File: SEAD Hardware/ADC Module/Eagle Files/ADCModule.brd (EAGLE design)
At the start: 48.9 x 67.6 mm, 51 parts, among them U1 ADS8568_PM_64, U2 LP2950-3.3ACZ

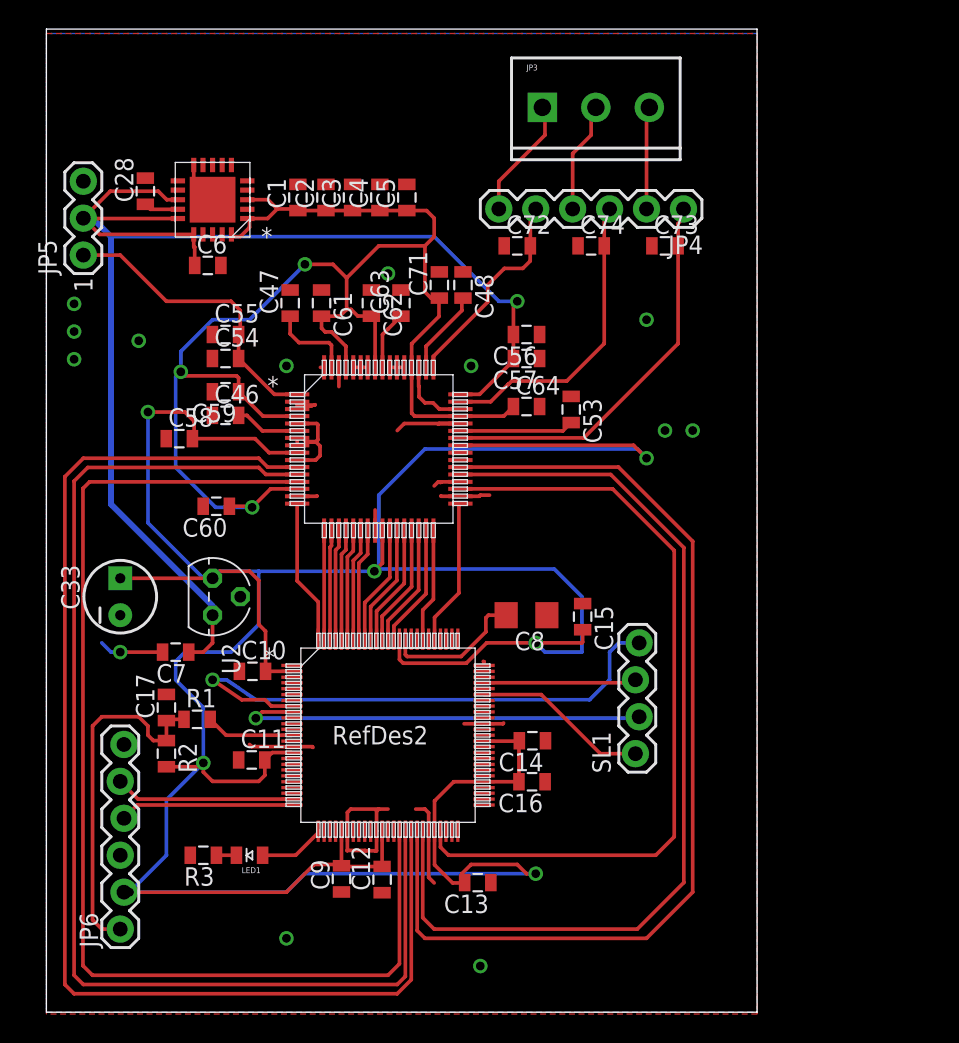
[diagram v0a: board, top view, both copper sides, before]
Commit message: Finished ADC Module v1.2 and reorganized file directories.
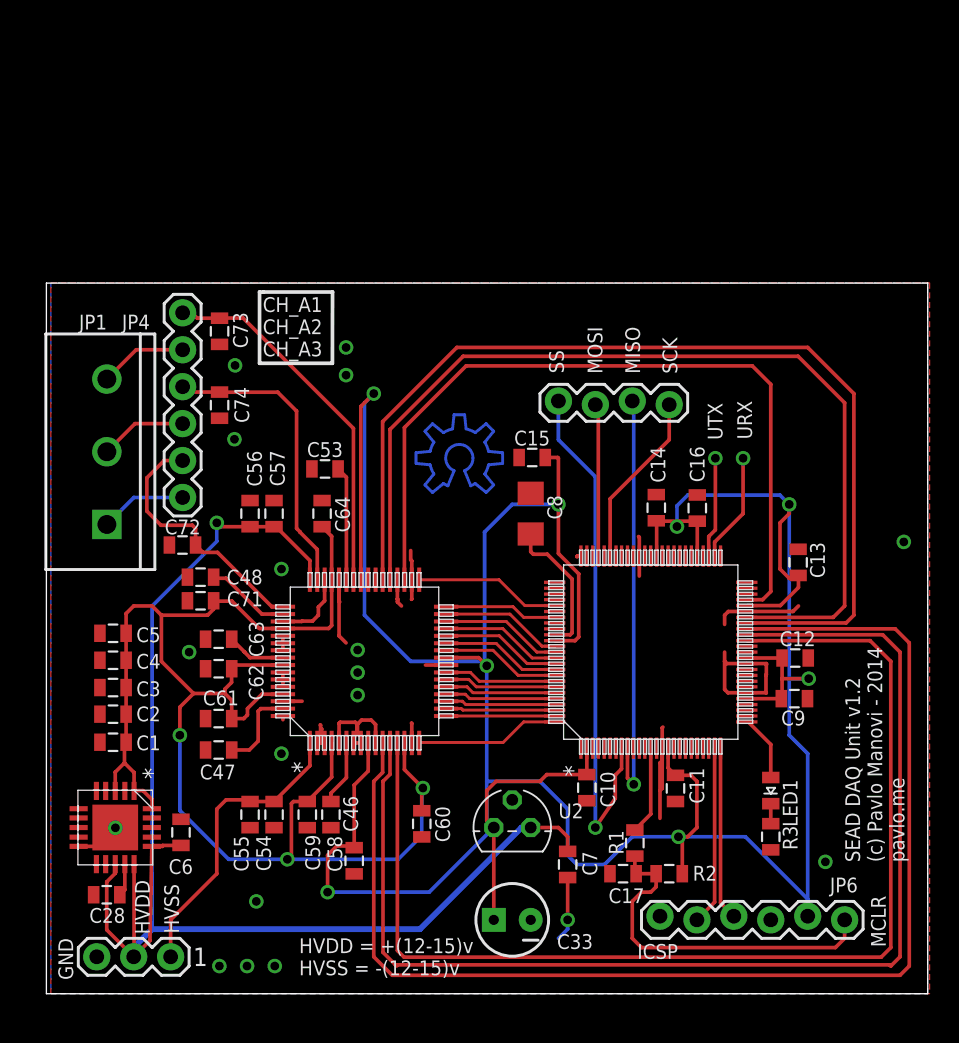
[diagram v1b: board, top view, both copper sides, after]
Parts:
- removed JP3: M03SCREW_LOCK, ASL:SCREWTERMINAL-3.5MM-3_LOCK.007S
- added JP1: M03-SCREW-5MM, ASL:SCREWTERMINAL-5MM-3
- moved JP5 50.9 mm to (6.00, 2.54), turned to 180 degrees
- moved JP6 49.8 mm to (54.9, 5.08), turned to 180 degrees
- moved C28 48.5 mm to (4.15, 6.81), turned to 180 degrees
- moved U$3 43.7 mm to (4.74, 11.4), turned to 270 degrees
- moved C1 39.6 mm to (4.58, 17.3), turned to 180 degrees
- moved R3 39.0 mm to (49.8, 10.8), turned to 270 degrees
- moved C6 39.0 mm to (9.26, 11.1), turned to 90 degrees
- moved C2 38.4 mm to (4.58, 19.2), turned to 180 degrees
- moved C3 37.5 mm to (4.58, 21.1), turned to 180 degrees
- moved C4 36.7 mm to (4.58, 22.9), turned to 180 degrees
- moved C5 36.1 mm to (4.58, 24.8), turned to 180 degrees
- moved LED1 36.1 mm to (49.8, 14.0), turned to 270 degrees
- moved R2 35.6 mm to (42.8, 8.26), turned to 0 degrees
- moved C33 34.9 mm to (32.0, 5.08), turned to 180 degrees
- moved C9 33.5 mm to (51.4, 20.3), turned to 180 degrees
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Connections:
- new net RX1A: U$1.52
- new net TX1A: U$1.53
- net N$1: now also JP1.3; no longer JP3.3
- net N$2: now also JP1.2; no longer JP3.2
- net N$3: now also JP1.1; no longer JP3.1
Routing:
- net N$5: track 0.00 -> 28.4 mm
- net VDD3V3_D: track 252.0 -> 237.1 mm, vias 7 -> 8
- net RX1A: track 0.00 -> 7.54 mm, vias 0 -> 1
- net TX1A: track 0.00 -> 6.92 mm, vias 0 -> 1
- net GND: track 66.2 -> 71.2 mm, vias 13 -> 18
- net AA3_R_OUT: track 14.6 -> 18.0 mm
- net N$3: track 8.37 -> 5.98 mm
- net SS: track 38.6 -> 36.5 mm
- net N$2: track 7.65 -> 6.01 mm
- net AA1_R_OUT: track 27.1 -> 25.5 mm
- net VDD5V0_A: track 104.8 -> 106.0 mm
- net N$1: track 7.06 -> 6.04 mm
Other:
- board size 48.9 x 67.6 mm -> 60.6 x 48.9 mm
- board text added: "CH_A1 CH_A2 CH_A3"
- board text added: "GND"
- board text added: "HVDD"
- board text added: "HVDD = +(12-15)v HVSS = -(12-15)v"
- board text added: "HVSS"
- board text added: "ICSP"
- board text added: "MCLR"
- board text added: "MISO"
- board text added: "MOSI"
- board text added: "Released under the TAPR OHL v1.0 - http://www.tapr.org/OHL"
- board text added: "SCK"
- board text added: "SEAD DAQ Unit v1.2 (c) Pavlo Manovi - 2014 pavlo.me"
- board text added: "SS"
- board text added: "URX"
- board text added: "UTX"

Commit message: Started SPI/USB Bridge
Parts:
- added C18: 10nF, SensorCape:0805
- added C19, C20: 47pF, SensorCape:0805
- added C21, C23, C24: 100nF, SensorCape:0805
- added C22: 4.7uF, SensorCape:CPOL-RADIAL-10UF-25V
- added L1: Ferrite Bead 0805, ASL:0805
- added R4, R5: 27 1%, SensorCape:0805
- added U$2: FT121Q, SensorCape:QFN16
- added U3: SI8663BC-B-IS1, SensorCape:SOIC-16
- added X1: MINI-USB-SCHIELD-32005-201, con-cypressindustries:32005-201
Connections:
- new net GND_USB: C18.2, C19.1, C20.2, C21.1, C22.2, C23.1, U$2.12, U$2.2, U3.8, X1.5
- new net N$10: R4.2, U$2.13
- new net N$11: X1.M1, X1.M2, X1.M3, X1.M4
- new net N$12: R5.2, U$2.14
- new net N$13: U$2.6, U3.4
- new net N$17: U$2.7, U3.7
- new net N$18: U$2.16, U3.5
- new net N$6: C18.1, L1.1, X1.1
- new net N$8: C19.2, R4.1, X1.2
- new net N$9: C20.1, R5.1, X1.3
- new net SCLK: U3.12
- new net VCC3V3_USB: C21.2, C24.1, C24.2, U$2.10, U$2.3, U$2.8, U$2.9, U3.1
- new net VCC_USB: C22.1, C23.2, L1.2, U$2.11
- net MISO: now also U3.13
- net MOSI: now also U3.10
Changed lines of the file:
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@@
 <layer number="97" name="Info" color="7" fill="1" visible="no" active="no"/>
 <layer number="98" name="Guide" color="6" fill="1" visible="no" active="no"/>
+<layer number="99" name="SpiceOrder" color="5" fill="1" visible="no" active="no"/>
 <layer number="100" name="Muster" color="7" fill="1" visible="no" active="no"/>
 <layer number="101" name="Patch_Top" color="12" fill="4" visible="yes" active="yes"/>
@@
 <attribute name="VALUE" x="2.89" y="31.005" size="0.4064" layer="27" rot="R90"/>
 </element>
+<element name="U$2" library="SensorCape" package="QFN16" value="FT121Q" x="-5.29" y="4.42"/>
+<element name="U3" library="SensorCape" package="SOIC-16" value="SI8663BC-B-IS1" x="-11.52" y="4.88"/>
+<element name="X1" library="con-cypressindustries" package="32005-201" value="MINI-USB-SCHIELD-32005-201" x="-20.7" y="7.35">
+<attribute name="OC_NEWARK" value="unknown" x="-20.7" y="7.35" size="1.778" layer="27" display="off"/>
+<attribute name="MPN" value="" x="-20.7" y="7.35" size="1.778" layer="27" display="off"/>
+<attribute name="MF" value="" x="-20.7" y="7.35" size="1.778" layer="27" display="off"/>
+<attribute name="OC_FARNELL" value="unknown" x="-20.7" y="7.35" size="1.778" layer="27" display="off"/>
+</element>
+<element name="L1" library="ASL" package="0805" value="Ferrite Bead 0805" x="-25.14" y="-2.68"/>
+<element name="C18" library="SensorCape" package="0805" value="10nF" x="-25.14" y="-6.23"/>
+<element name="R4" library="SensorCape" package="0805" value="27 1%" x="-25.14" y="-16.88"/>
+<element name="R5" library="SensorCape" package="0805" value="27 1%" x="-25.14" y="-20.43"/>
+<element name="C22" library="SensorCape" package="CPOL-RADIAL-10UF-25V" value="4.7uF" x="-32.13" y="-20.8"/>
+<element name="C23" library="SensorCape" package="0805" value="100nF" x="-33.2" y="-27.53"/>
+<element name="C19" library="SensorCape" package="0805" value="47pF" x="-33.2" y="-31.08"/>
+<element name="C20" library="SensorCape" package="0805" value="47pF" x="-33.2" y="-34.63"/>
+<element name="C21" library="SensorCape" package="0805" value="100nF" x="-33.2" y="-38.18"/>
+<element name="C24" library="SensorCape" package="0805" value="100nF" x="-33.2" y="-42.62"/>
 </elements>
 <signals>
@@
 <wire x1="37.9582" y1="30.099" x2="37.9582" y2="40.3098" width="0.254" layer="1"/>
 <wire x1="37.9582" y1="40.3098" x2="37.755" y2="40.513" width="0.254" layer="1"/>
+<contactref element="U3" pad="10"/>
+<wire x1="-8.8276" y1="1.705" x2="37.9582" y2="30.099" width="0" layer="19" extent="1-1"/>
 </signal>
 <signal name="MISO">
@@
 <wire x1="40.3966" y1="14.4018" x2="40.3966" y2="40.6654" width="0.254" layer="16"/>
 <wire x1="40.3966" y1="40.6654" x2="40.295" y2="40.767" width="0.254" layer="16"/>
+<contactref element="U3" pad="13"/>
+<wire x1="-8.8276" y1="5.515" x2="39.9648" y2="14.8336" width="0" layer="19" extent="1-1"/>
 </signal>
 <signal name="SS">
@@
 <wire x1="28.041234375" y1="35.9738625" x2="27.610715625" y2="34.9345" width="0.2" layer="16"/>
 </signal>
+<signal name="N$6">
+<contactref element="X1" pad="1"/>
+<contactref element="L1" pad="1"/>
+<contactref element="C18" pad="1"/>
+<wire x1="-26.04" y1="-2.68" x2="-26.04" y2="-6.23" width="0" layer="19" extent="1-1"/>
+<wire x1="-17.7" y1="8.95" x2="-26.04" y2="-2.68" width="0" layer="19" extent="1-1"/>
+</signal>
+<signal name="N$8">
+<contactref element="X1" pad="2"/>
+<contactref element="R4" pad="1"/>
+<contactref element="C19" pad="2"/>
+<wire x1="-26.04" y1="-16.88" x2="-32.3" y2="-31.08" width="0" layer="19" extent="1-1"/>
+<wire x1="-17.7" y1="8.15" x2="-26.04" y2="-16.88" width="0" layer="19" extent="1-1"/>
+</signal>
+<signal name="N$9">
+<contactref element="X1" pad="3"/>
+<contactref element="R5" pad="1"/>
+<contactref element="C20" pad="1"/>
+<wire x1="-26.04" y1="-20.43" x2="-34.1" y2="-34.63" width="0" layer="19" extent="1-1"/>
+<wire x1="-17.7" y1="7.35" x2="-26.04" y2="-20.43" width="0" layer="19" extent="1-1"/>
+</signal>
+<signal name="N$11">
+<contactref element="X1" pad="M4"/>
+<contactref element="X1" pad="M3"/>
+<contactref element="X1" pad="M2"/>
+<contactref element="X1" pad="M1"/>
+<wire x1="-17.8" y1="2.9" x2="-23.7" y2="2.9" width="0" layer="19" extent="1-1"/>
+<wire x1="-23.7" y1="11.8" x2="-23.7" y2="2.9" width="0" layer="19" extent="1-1"/>
+<wire x1="-17.8" y1="11.8" x2="-23.7" y2="11.8" width="0" layer="19" extent="1-1"/>
+</signal>
+<signal name="VCC_USB">
+<contactref element="L1" pad="2"/>
+<contactref element="U$2" pad="11"/>
+<contactref element="C23" pad="2"/>
+<contactref element="C22" pad="1"/>
+<wire x1="-30.86" y1="-20.8" x2="-32.3" y2="-27.53" width="0" layer="19" extent="1-1"/>
+<wire x1="-24.24" y1="-2.68" x2="-30.86" y2="-20.8" width="0" layer="19" extent="1-1"/>
+<wire x1="-3.365" y1="4.745" x2="-24.24" y2="-2.68" width="0" layer="19" extent="1-1"/>
+</signal>
+<signal name="VCC3V3_USB">
+<contactref element="U$2" pad="8"/>
+<contactref element="U$2" pad="9"/>
+<contactref element="U$2" pad="3"/>
+<contactref element="U$2" pad="10"/>
+<contactref element="C21" pad="2"/>
+<contactref element="U3" pad="1"/>
+<contactref element="C24" pad="2"/>
+<contactref element="C24" pad="1"/>
+<wire x1="-32.3" y1="-42.62" x2="-34.1" y2="-42.62" width="0" layer="19" extent="1-1"/>
+<wire x1="-32.3" y1="-38.18" x2="-32.3" y2="-42.62" width="0" layer="19" extent="1-1"/>
+<wire x1="-7.215" y1="4.095" x2="-32.3" y2="-38.18" width="0" layer="19" extent="1-1"/>
+<wire x1="-4.315" y1="2.495" x2="-7.215" y2="4.095" width="0" layer="19" extent="1-1"/>
+<wire x1="-3.365" y1="3.445" x2="-4.315" y2="2.495" width="0" layer="19" extent="1-1"/>
+<wire x1="-3.365" y1="4.095" x2="-3.365" y2="3.445" width="0" layer="19" extent="1-1"/>
+<wire x1="-14.2124" y1="9.325" x2="-7.215" y2="4.095" width="0" layer="19" extent="1-1"/>
+</signal>
+<signal name="GND_USB">
+<contactref element="C23" pad="1"/>
+<contactref element="C22" pad="2"/>
+<contactref element="C19" pad="1"/>
+<contactref element="C20" pad="2"/>
+<contactref element="X1" pad="5"/>
+<contactref element="C18" pad="2"/>
+<contactref element="U$2" pad="2"/>
+<contactref element="U$2" pad="12"/>
+<contactref element="C21" pad="1"/>
+<contactref element="U3" pad="8"/>
+<wire x1="-32.3" y1="-34.63" x2="-34.1" y2="-38.18" width="0" layer="19" extent="1-1"/>
+<wire x1="-34.1" y1="-31.08" x2="-32.3" y2="-34.63" width="0" layer="19" extent="1-1"/>
+<wire x1="-34.1" y1="-27.53" x2="-34.1" y2="-31.08" width="0" layer="19" extent="1-1"/>
+<wire x1="-33.4" y1="-20.8" x2="-34.1" y2="-27.53" width="0" layer="19" extent="1-1"/>
+<wire x1="-24.24" y1="-6.23" x2="-33.4" y2="-20.8" width="0" layer="19" extent="1-1"/>
+<wire x1="-14.2124" y1="0.435" x2="-24.24" y2="-6.23" width="0" layer="19" extent="1-1"/>
+<wire x1="-17.7" y1="5.75" x2="-14.2124" y2="0.435" width="0" layer="19" extent="1-1"/>
+<wire x1="-7.215" y1="4.745" x2="-14.2124" y2="0.435" width="0" layer="19" extent="1-1"/>
+<wire x1="-3.365" y1="5.395" x2="-7.215" y2="4.745" width="0" layer="19" extent="1-1"/>
+</signal>
+<signal name="N$10">
+<contactref element="R4" pad="2"/>
+<contactref element="U$2" pad="13"/>
+<wire x1="-4.315" y1="6.345" x2="-24.24" y2="-16.88" width="0" layer="19" extent="1-1"/>
+</signal>
+<signal name="N$12">
+<contactref element="U$2" pad="14"/>
+<contactref element="R5" pad="2"/>
+<wire x1="-4.965" y1="6.345" x2="-24.24" y2="-20.43" width="0" layer="19" extent="1-1"/>
+</signal>
+<signal name="N$13">
+<contactref element="U$2" pad="6"/>
+<contactref element="U3" pad="4"/>
+<wire x1="-5.615" y1="2.495" x2="-14.2124" y2="5.515" width="0" layer="19" extent="1-1"/>
+</signal>
+<signal name="N$17">
+<contactref element="U$2" pad="7"/>
+<contactref element="U3" pad="7"/>
+<wire x1="-4.965" y1="2.495" x2="-14.2124" y2="1.705" width="0" layer="19" extent="1-1"/>
+</signal>
+<signal name="N$18">
+<contactref element="U3" pad="5"/>
+<contactref element="U$2" pad="16"/>
+<wire x1="-6.265" y1="6.345" x2="-14.2124" y2="4.245" width="0" layer="19" extent="1-1"/>
+</signal>
+<signal name="SCLK">
+<contactref element="U3" pad="12"/>
+</signal>
 </signals>

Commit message: Finished DAQ Hardware v1.4 and Filtering Simulations
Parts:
- removed C72, C73, C74: 10nF, SensorCape:0805
- removed JP4: (no value), ASL:1X06
- removed JP5: M03PTH, ASL:1X03
- removed L1: Ferrite Bead 0805, ASL:0805
- removed R4, R5: 27 1%, SensorCape:0805
- removed U3: SI8663BC-B-IS1, SensorCape:SOIC-16
- removed X1: MINI-USB-SCHIELD-32005-201, con-cypressindustries:32005-201
- added C25, C26, C27, C29, C32: 10uF, ASL:0805
- added C30: 1uF, SensorCape:0805
- added C31: 10nF, SensorCape:0805
- added C34: 10uF, SensorCape:1206
- added JP2: M03-SCREW-5MM, ASL:SCREWTERMINAL-5MM-3
- added R23: 1.5M, ASL:0805
- added R24: 162k, ASL:0805
- added U6: TPS7A3301_RGW_20, SensorCape:RGW20_3P15X3P15
- C18: value 10nF -> 1uF
- C19: value 47pF -> 10uF; device SensorCape:0805 -> SensorCape:1206
- C20: value 47pF -> 10uF; device SensorCape:0805 -> ASL:0805
- C21, C23, C24: value 100nF -> 10uF; device SensorCape:0805 -> ASL:0805
- C22: value 4.7uF -> 10uF; device SensorCape:CPOL-RADIAL-10UF-25V -> ASL:0805
- U$2: value FT121Q -> TPS7A4700_RGW_20; device SensorCape:QFN16 -> SensorCape:RGW20_3P15X3P15
- moved C24 89.5 mm to (19.5, 29.7), turned to 90 degrees
- moved C21 87.0 mm to (21.3, 29.7), turned to 90 degrees
- moved C20 82.0 mm to (17.7, 29.7), turned to 90 degrees
- moved C23 75.5 mm to (16.0, 29.7), turned to 90 degrees
- moved C22 74.8 mm to (23.0, 29.7), turned to 90 degrees
- moved C19 71.1 mm to (2.07, 30.7), turned to 90 degrees
- moved C18 49.2 mm to (4.82, 32.8), turned to 90 degrees
- moved U$2 30.2 mm to (11.4, 29.6), turned to 180 degrees
- moved C5 20.8 mm to (25.0, 20.9), turned to 90 degrees
- moved C63 19.3 mm to (31.1, 23.9)
- moved C12 19.3 mm to (70.8, 23.1)
- moved C13 19.3 mm to (71.0, 29.7)
- moved C14 19.3 mm to (61.2, 33.4)
- moved C17 19.3 mm to (59.0, 8.26)
- moved C33 19.3 mm to (51.3, 5.08)
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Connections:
- removed net AA1_R_OUT: C73.2, JP4.1, U1.42
- removed net AA2_R_OUT: C74.2, JP4.3, U1.47
- removed net AA3_R_OUT: C72.2, JP4.5, U1.49
- removed net GND_USB: C18.2, C19.1, C20.2, C21.1, C22.2, C23.1, U$2.12, U$2.2, U3.8, X1.5
- removed net N$1: JP1.3, JP4.2
- removed net N$10: R4.2, U$2.13
- removed net N$11: X1.M1, X1.M2, X1.M3, X1.M4
- removed net N$12: R5.2, U$2.14
- removed net N$13: U$2.6, U3.4
- removed net N$17: U$2.7, U3.7
- removed net N$18: U$2.16, U3.5
- removed net N$2: JP1.2, JP4.4
- removed net N$3: JP1.1, JP4.6
- removed net N$9: C20.1, R5.1, X1.3
- removed net SCLK: U3.12
- removed net VCC3V3_USB: C21.2, C24.1, C24.2, U$2.10, U$2.3, U$2.8, U$2.9, U3.1
- removed net VCC_USB: C22.1, C23.2, L1.2, U$2.11
- new net A0: JP1.3, U1.42
- new net A1: JP1.2, U1.47
- new net B0: JP1.1, U1.49
- new net B1: JP2.3, U1.54
- new net C0: JP2.2, U1.64
- new net C1: JP2.1, U1.59
- new net D0: U1.7
- new net D1: U1.2
- new net HVDD_15D: C19.1, U$2.13, U$2.15, U$2.16
- new net HVSS_15D: C34.2, U6.13, U6.15, U6.16
- new net N$33: C30.1, U6.14
- net GND: now also C18.2, C19.2, C20.2, C21.2, C22.2, C23.2, C24.2, C25.2, C26.2, C27.2, C29.2, C30.2, C32.2, C34.1, R24.1, U$2.11, U$2.21, U$2.4, U$2.6, U$2.7, U$2.9, U6.21, U6.7; no longer C72.1, C73.1, C74.1, JP5.3, U1.2, U1.54, U1.59, U1.64, U1.7
- net HVDD_12A: now also C20.1, C21.1, C22.1, C23.1, C24.1, U$2.1, U$2.20, U$2.3; no longer JP5.2
- net HVSS_12A: now also C25.1, C26.1, C27.1, C29.1, C31.1, C32.1, R23.2, U6.1, U6.20; no longer JP5.1
- net MISO: no longer U3.13
- net MOSI: no longer U3.10
- net N$6: now also U$2.14; no longer L1.1, X1.1
- net N$8: now also C31.2, R23.1, R24.2, U6.3; no longer C19.2, R4.1, X1.2
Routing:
- net B0: track 0.00 -> 59.7 mm, vias 0 -> 2
- net A1: track 0.00 -> 46.3 mm, vias 0 -> 1
- net A0: track 0.00 -> 43.2 mm
- net C0: track 0.00 -> 37.1 mm, vias 0 -> 3
- net C1: track 0.00 -> 34.9 mm, vias 0 -> 2
- net B1: track 0.00 -> 27.1 mm, vias 0 -> 1
- net AA1_R_OUT: track 25.5 -> 0.00 mm
- net HVSS_12A: track 20.8 -> 45.6 mm, vias 0 -> 2
- net AA2_R_OUT: track 20.7 -> 0.00 mm
- net AA3_R_OUT: track 18.0 -> 0.00 mm
- net HVDD_12A: track 97.7 -> 115.1 mm, vias 1 -> 2
- net VDD3V3_D: track 237.1 -> 226.2 mm, vias 8 -> 9
- net N$8: track 0.00 -> 10.1 mm
- net N$33: track 0.00 -> 8.98 mm, vias 0 -> 2
- net GND: track 71.2 -> 79.1 mm, vias 18 -> 81
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- added copper zone on layer 1, net HVDD_12A
- added copper zone on layer 1, net HVDD_15D
- added copper zone on layer 1, net HVSS_15D
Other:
- board size 60.6 x 48.9 mm -> 79.9 x 48.9 mm
- board text removed: "CH_A1 CH_A2 CH_A3"
- board text removed: "GND"
- board text removed: "HVDD"
- board text removed: "HVDD = +(12-15)v HVSS = -(12-15)v"
- board text removed: "HVSS"
